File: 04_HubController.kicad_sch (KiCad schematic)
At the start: 79 parts, among them U16 CYUSB3304-68LTXx, Y1 26MHz

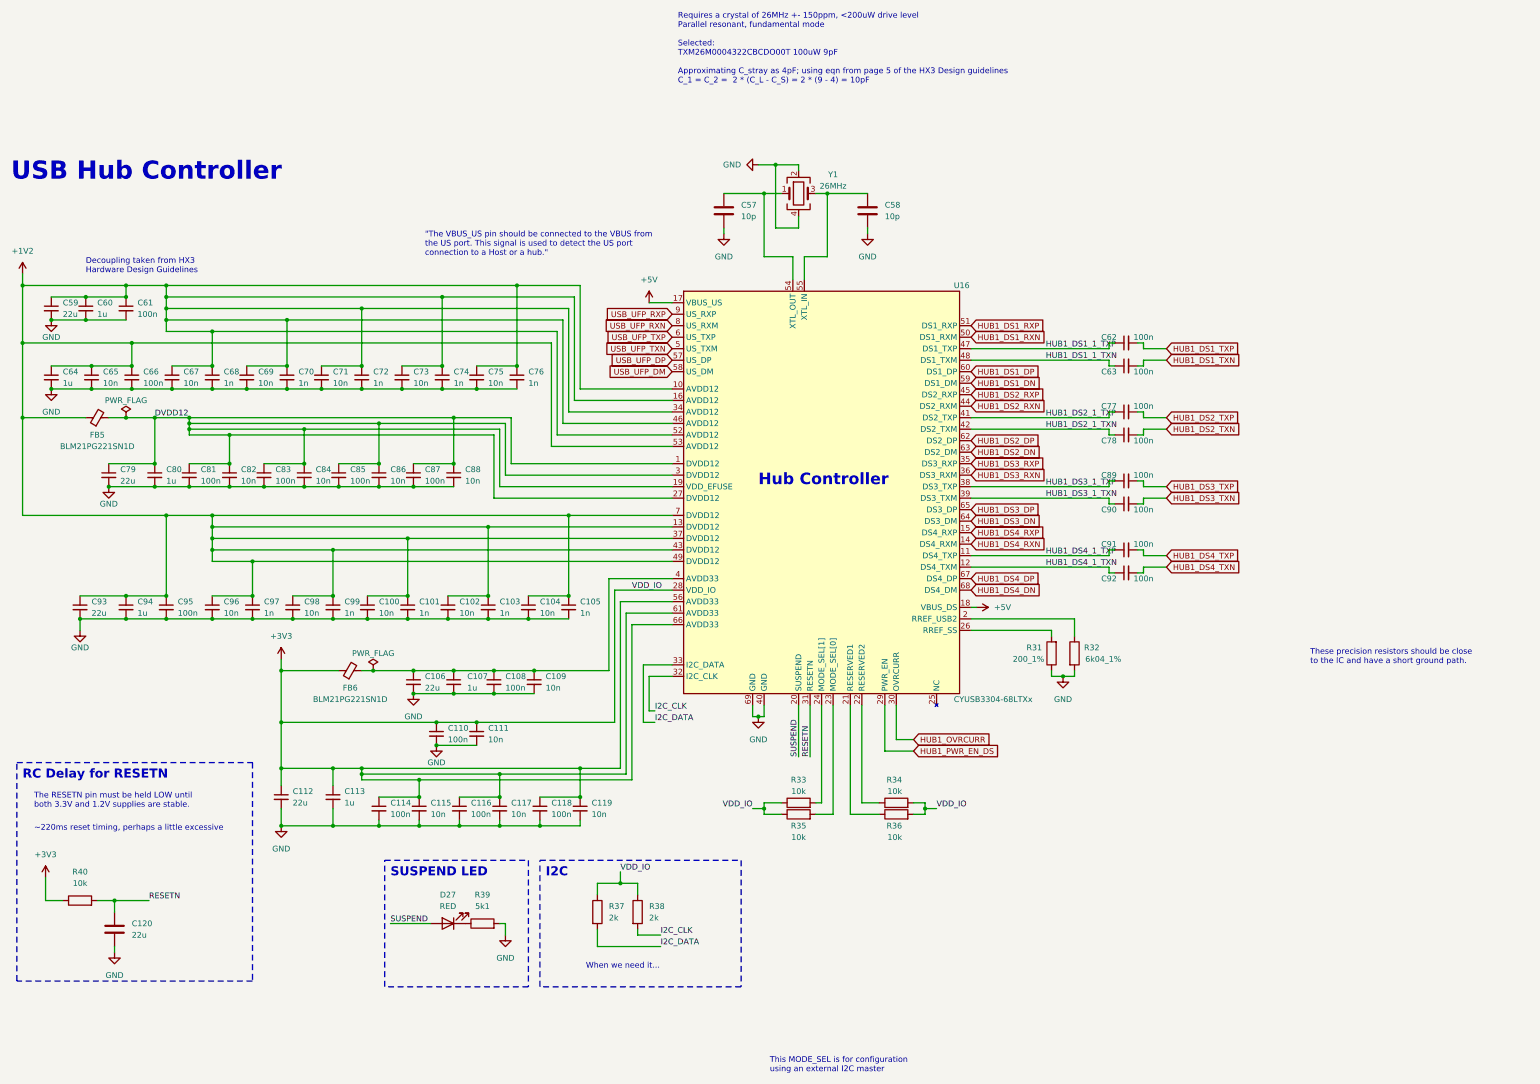
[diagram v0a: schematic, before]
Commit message: route power delivery controller
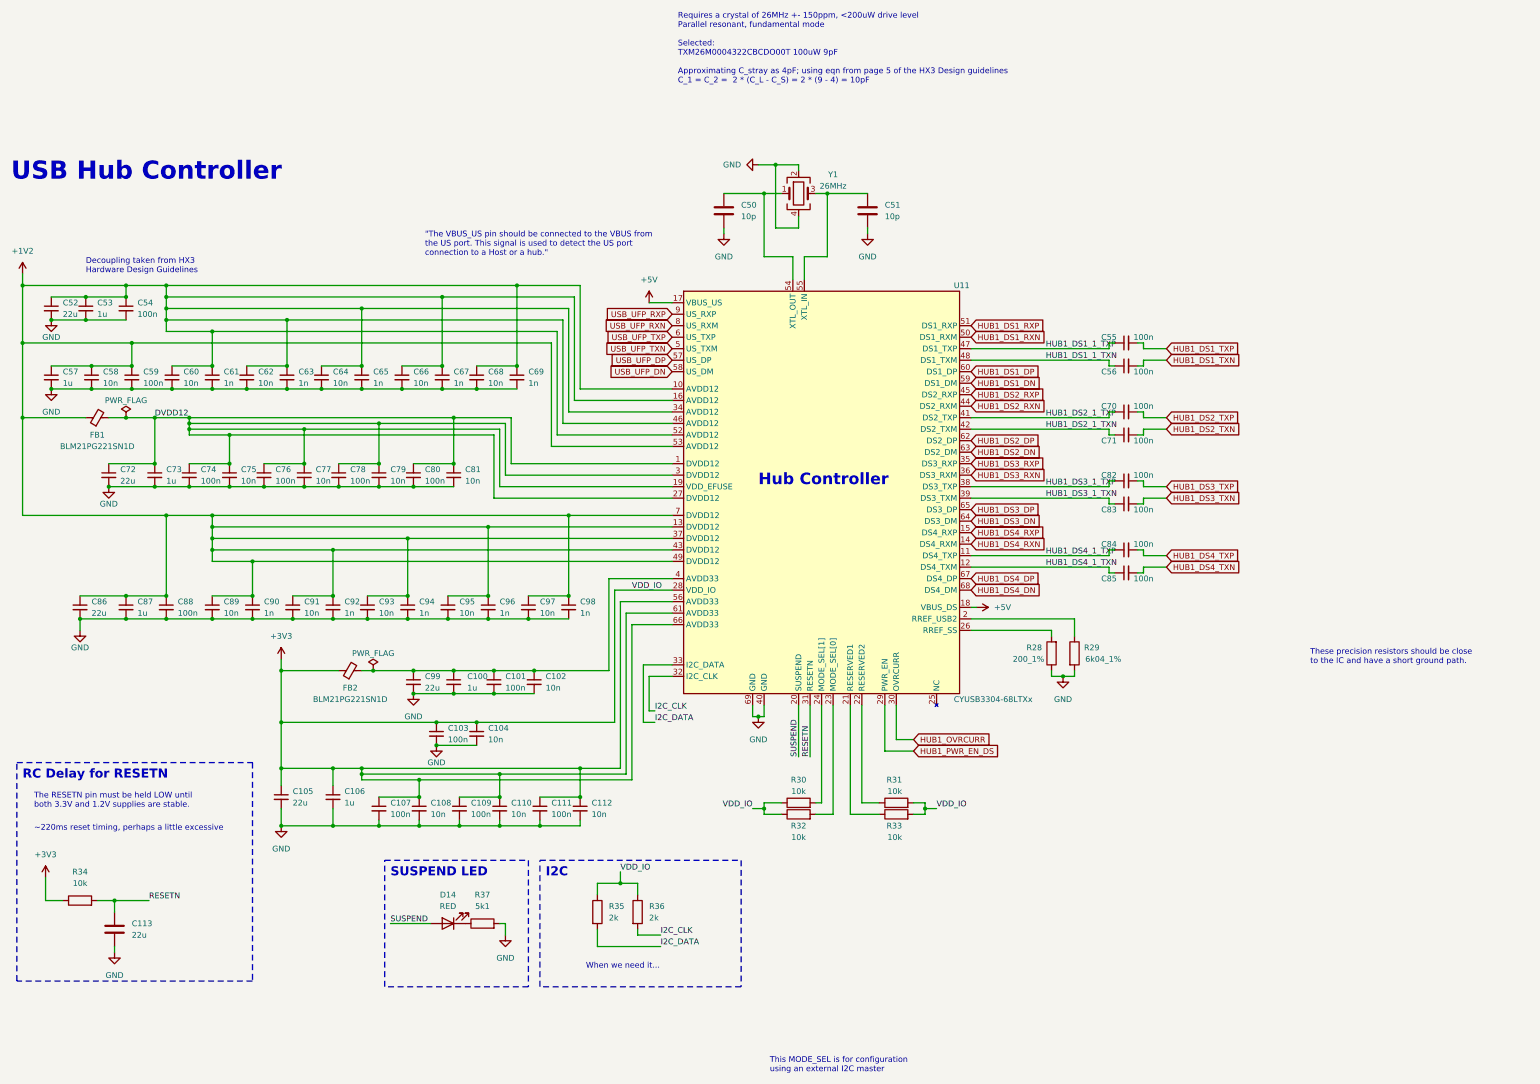
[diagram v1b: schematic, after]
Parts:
- renumbered C107 to C100, C108 to C101, C109 to C102, C110 to C103, C111 to C104, C112 to C105, C113 to C106, C114 to C107, C115 to C108, C116 to C109, C117 to C110, C118 to C111, C119 to C112, C120 to C113, C57 to C50, C58 to C51, C59 to C52, C60 to C53, C61 to C54, C62 to C55, C63 to C56, C64 to C57, C65 to C58, C66 to C59, C67 to C60, C68 to C61, C69 to C62, C70 to C63, C71 to C64, C72 to C65, C73 to C66, C74 to C67, C75 to C68, C76 to C69, C77 to C70, C78 to C71, C79 to C72, C80 to C73, C81 to C74, C82 to C75, C83 to C76, C84 to C77, C85 to C78, C86 to C79, C87 to C80, C88 to C81, C89 to C82, C90 to C83, C91 to C84, C92 to C85, C93 to C86, C94 to C87, C95 to C88, C96 to C89, C97 to C90, C98 to C91, C99 to C92, C100 to C93, C101 to C94, C102 to C95, C103 to C96, C104 to C97, C105 to C98, C106 to C99, D27 to D14, FB5 to FB1, FB6 to FB2, R31 to R28, R32 to R29, R33 to R30, R34 to R31, R35 to R32, R36 to R33, R40 to R34, R37 to R35, R38 to R36, R39 to R37, U16 to U11
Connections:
- net USB_UFP_DM renamed USB_UFP_DN

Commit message: settle on a layout
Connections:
- net HUB1_DS1_RXN: now also U11.51 (DS1_RXP); no longer U11.50 (DS1_RXM)
- net HUB1_DS1_RXP: now also U11.50 (DS1_RXM); no longer U11.51 (DS1_RXP)
- net HUB1_DS2_RXN: now also U11.45 (DS2_RXP); no longer U11.44 (DS2_RXM)
- net HUB1_DS2_RXP: now also U11.44 (DS2_RXM); no longer U11.45 (DS2_RXP)
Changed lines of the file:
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@@
-    )
-  )
-  (global_label "HUB1_DS1_RXN" (shape input) (at 224.79 53.34 0) (fields_autoplaced)
-    (effects (font (size 1.27 1.27)) (justify left))
-    (property "Intersheetrefs" "${INTERSHEET_REFS}" (at 242.3499 53.34 0)
-      (effects (font (size 1.27 1.27)) (justify left) hide)
     )
   )
@@
     )
   )
+  (global_label "HUB1_DS1_RXP" (shape input) (at 224.79 53.34 0) (fields_autoplaced)
+    (effects (font (size 1.27 1.27)) (justify left))
+    (property "Intersheetrefs" "${INTERSHEET_REFS}" (at 242.2894 53.34 0)
+      (effects (font (size 1.27 1.27)) (justify left) hide)
+    )
+  )
   (global_label "HUB1_DS1_DP" (shape input) (at 224.79 60.96 0) (fields_autoplaced)
     (effects (font (size 1.27 1.27)) (justify left))
     (property "Intersheetrefs" "${INTERSHEET_REFS}" (at 241.0799 60.96 0)
-      (effects (font (size 1.27 1.27)) (justify left) hide)
-    )
-  )
-  (global_label "HUB1_DS2_RXN" (shape input) (at 224.79 68.58 0) (fields_autoplaced)
-    (effects (font (size 1.27 1.27)) (justify left))
-    (property "Intersheetrefs" "${INTERSHEET_REFS}" (at 242.3499 68.58 0)
       (effects (font (size 1.27 1.27)) (justify left) hide)
     )
@@
     (property "Intersheetrefs" "${INTERSHEET_REFS}" (at 142.8834 53.34 0)
       (effects (font (size 1.27 1.27)) (justify right) hide)
+    )
+  )
+  (global_label "HUB1_DS1_RXN" (shape input) (at 224.79 50.8 0) (fields_autoplaced)
+    (effects (font (size 1.27 1.27)) (justify left))
+    (property "Intersheetrefs" "${INTERSHEET_REFS}" (at 242.3499 50.8 0)
+      (effects (font (size 1.27 1.27)) (justify left) hide)
+    )
+  )
+  (global_label "HUB1_DS2_RXP" (shape input) (at 224.79 68.58 0) (fields_autoplaced)
+    (effects (font (size 1.27 1.27)) (justify left))
+    (property "Intersheetrefs" "${INTERSHEET_REFS}" (at 242.2894 68.58 0)
+      (effects (font (size 1.27 1.27)) (justify left) hide)
     )
   )
@@
     )
   )
-  (global_label "HUB1_DS1_RXP" (shape input) (at 224.79 50.8 0) (fields_autoplaced)
-    (effects (font (size 1.27 1.27)) (justify left))
-    (property "Intersheetrefs" "${INTERSHEET_REFS}" (at 242.2894 50.8 0)
-      (effects (font (size 1.27 1.27)) (justify left) hide)
-    )
-  )
   (global_label "HUB1_DS2_DP" (shape input) (at 224.79 76.2 0) (fields_autoplaced)
     (effects (font (size 1.27 1.27)) (justify left))
@@
     (effects (font (size 1.27 1.27)) (justify left))
     (property "Intersheetrefs" "${INTERSHEET_REFS}" (at 285.2275 88.9 0)
+      (effects (font (size 1.27 1.27)) (justify left) hide)
+    )
+  )
+  (global_label "HUB1_DS2_RXN" (shape input) (at 224.79 66.04 0) (fields_autoplaced)
+    (effects (font (size 1.27 1.27)) (justify left))
+    (property "Intersheetrefs" "${INTERSHEET_REFS}" (at 242.3499 66.04 0)
       (effects (font (size 1.27 1.27)) (justify left) hide)
     )
@@
       (effects (font (size 1.27 1.27)) (justify left) hide)
     )
-  )
-  (global_label "HUB1_DS2_RXP" (shape input) (at 224.79 66.04 0) (fields_autoplaced)
-    (effects (font (size 1.27 1.27)) (justify left))
-    (property "Intersheetrefs" "${INTERSHEET_REFS}" (at 242.2894 66.04 0)
-      (effects (font (size 1.27 1.27)) (justify left) hide)
-    )

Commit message: finish layout draft
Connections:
- net HUB1_DS4_RXN: now also U11.15 (DS4_RXP); no longer U11.14 (DS4_RXM)
- net HUB1_DS4_RXP: now also U11.14 (DS4_RXM); no longer U11.15 (DS4_RXP)
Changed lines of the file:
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@@
-    )
-  )
-  (global_label "HUB1_DS4_RXN" (shape input) (at 224.79 99.06 0) (fields_autoplaced)
-    (effects (font (size 1.27 1.27)) (justify left))
-    (property "Intersheetrefs" "${INTERSHEET_REFS}" (at 242.3499 99.06 0)
-      (effects (font (size 1.27 1.27)) (justify left) hide)
     )
   )
@@
     )
   )
+  (global_label "HUB1_DS4_RXN" (shape input) (at 224.79 96.52 0) (fields_autoplaced)
+    (effects (font (size 1.27 1.27)) (justify left))
+    (property "Intersheetrefs" "${INTERSHEET_REFS}" (at 242.3499 96.52 0)
+      (effects (font (size 1.27 1.27)) (justify left) hide)
+    )
+  )
   (global_label "HUB1_DS4_DN" (shape input) (at 224.79 109.22 0) (fields_autoplaced)
     (effects (font (size 1.27 1.27)) (justify left))
@@
     )
   )
+  (global_label "HUB1_DS4_RXP" (shape input) (at 224.79 99.06 0) (fields_autoplaced)
+    (effects (font (size 1.27 1.27)) (justify left))
+    (property "Intersheetrefs" "${INTERSHEET_REFS}" (at 242.2894 99.06 0)
+      (effects (font (size 1.27 1.27)) (justify left) hide)
+    )
+  )
   (global_label "HUB1_DS3_RXN" (shape input) (at 224.79 83.82 0) (fields_autoplaced)
     (effects (font (size 1.27 1.27)) (justify left))
     (property "Intersheetrefs" "${INTERSHEET_REFS}" (at 242.3499 83.82 0)
-      (effects (font (size 1.27 1.27)) (justify left) hide)
-    )
-  )
-  (global_label "HUB1_DS4_RXP" (shape input) (at 224.79 96.52 0) (fields_autoplaced)
-    (effects (font (size 1.27 1.27)) (justify left))
-    (property "Intersheetrefs" "${INTERSHEET_REFS}" (at 242.2894 96.52 0)
       (effects (font (size 1.27 1.27)) (justify left) hide)
     )
@@
   )
   (symbol (lib_id "Device:C_Small") (at 100.33 113.03 0) (unit 1)
-    (in_bom yes) (on_board yes) (dnp no) (fields_autoplaced)
+    (in_bom yes) (on_board yes) (dnp no)
     (property "Reference" "C94" (at 102.87 111.7663 0)
-      (effects (font (size 1.27 1.27)) (justify left))
+      (effects (font (size 1.27 1.27)) (justify right))
     )
     (property "Value" "1n" (at 102.87 114.3063 0)

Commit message: fixing drcs
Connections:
- net HUB1_OVRCURR is gone; now on net +3V3: U11.30 (OVRCURR)
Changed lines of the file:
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@@
+    (effects (font (size 1.27 1.27)) (justify left bottom))
+  )
+  (label "VDD_IO" (at 212.09 142.24 0) (fields_autoplaced)
     (effects (font (size 1.27 1.27)) (justify left bottom))
   )
@@
       (effects (font (size 1.27 1.27)) (justify left) hide)
     )
-  )
-  (global_label "HUB1_OVRCURR" (shape input) (at 212.09 142.24 0) (fields_autoplaced)
-    (effects (font (size 1.27 1.27)) (justify left))
-    (property "Intersheetrefs" "${INTERSHEET_REFS}" (at 230.0129 142.24 0)
-      (effects (font (size 1.27 1.27)) (justify left) hide)
-    )

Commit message: finish bom list
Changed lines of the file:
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@@
     (stroke (width 0) (type default))
   )
+  (wire (pts (xy 154.94 45.72) (xy 154.94 44.45))
+    (stroke (width 0) (type default))
+  )
   (wire (pts (xy 138.43 41.91) (xy 124.46 41.91))
     (stroke (width 0) (type default))
@@
     (stroke (width 0) (type default))
   )
-  (wire (pts (xy 153.67 45.72) (xy 158.75 45.72))
-    (stroke (width 0) (type default))
-  )
   (wire (pts (xy 138.43 160.02) (xy 138.43 161.29))
     (stroke (width 0) (type default))
@@
     (stroke (width 0) (type default))
   )
+  (wire (pts (xy 154.94 45.72) (xy 158.75 45.72))
+    (stroke (width 0) (type default))
+  )
   (wire (pts (xy 135.89 92.71) (xy 158.75 92.71))
     (stroke (width 0) (type default))
@@
   )
   (text "\"The VBUS_US pin should be connected to the VBUS from\nthe US port. This signal is used to detect the US port\nconnection to a Host or a hub.\""
-    (at 104.14 35.56 0)
+    (at 101.6 26.67 0)
     (effects (font (size 1.27 1.27)) (justify left bottom))
   )
@@
     )
   )
-  (symbol (lib_id "power:+5V") (at 153.67 45.72 0) (unit 1)
+  (symbol (lib_id "power:+5V") (at 154.94 44.45 0) (unit 1)
     (in_bom yes) (on_board yes) (dnp no) (fields_autoplaced)
-    (property "Reference" "#PWR060" (at 153.67 49.53 0)
+    (property "Reference" "#PWR060" (at 154.94 48.26 0)
       (effects (font (size 1.27 1.27)) hide)
     )
-    (property "Value" "+5V" (at 153.67 40.64 0)
+    (property "Value" "+5V" (at 154.94 39.37 0)
       (effects (font (size 1.27 1.27)))
     )
-    (property "Footprint" "" (at 153.67 45.72 0)
+    (property "Footprint" "" (at 154.94 44.45 0)
       (effects (font (size 1.27 1.27)) hide)
     )
-    (property "Datasheet" "" (at 153.67 45.72 0)
+    (property "Datasheet" "" (at 154.94 44.45 0)
       (effects (font (size 1.27 1.27)) hide)
     )
@@
     )
   )
-  (symbol (lib_id "power:GND") (at 27.94 118.11 0) (unit 1)
+  (symbol (lib_id "power:GND") (at 27.94 118.11 0) (mirror y) (unit 1)
     (in_bom yes) (on_board yes) (dnp no)
     (property "Reference" "#PWR065" (at 27.94 124.46 0)

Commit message: fix bom
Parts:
- added R50, R51: 10k, Resistor_SMD:R_0402_1005Metric, symbol Device:R_Small
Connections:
- net +5V: now also R50.1; no longer U11.17 (VBUS_US)
- net GND: now also R51.2
- new net: R50.2, R51.1, U11.17 (VBUS_US)
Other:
- note added: ""The VBUS_US pin should be connected to the VBUS from the US port. This signal is used to detect the US port connection to a Host or a hub." "It is recommended to connect a pair of resistors to the VBUS_US pin to discharge VBUS faster in case of a disconnection event" HX3 Hardware Design Guidelines page 8."
- note removed: ""The VBUS_US pin should be connected to the VBUS from the US port. This signal is used to detect the US port connection to a Host or a hub.""
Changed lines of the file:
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@@
   (junction (at 77.47 81.28) (diameter 0) (color 0 0 0 0)
   )
+  (junction (at 142.24 34.29) (diameter 0) (color 0 0 0 0)
+  )
   (junction (at 101.6 86.36) (diameter 0) (color 0 0 0 0)
   )
@@
     (stroke (width 0) (type default))
   )
-  (wire (pts (xy 154.94 45.72) (xy 154.94 44.45))
+  (wire (pts (xy 154.94 34.29) (xy 154.94 45.72))
     (stroke (width 0) (type default))
   )
@@
     (stroke (width 0) (type default))
   )
+  (wire (pts (xy 154.94 34.29) (xy 142.24 34.29))
+    (stroke (width 0) (type default))
+  )
   (wire (pts (xy 24.13 177.8) (xy 20.32 177.8))
     (stroke (width 0) (type default))
@@
     (effects (font (size 1.27 1.27)) (justify left bottom))
   )
-  (text "\"The VBUS_US pin should be connected to the VBUS from\nthe US port. This signal is used to detect the US port\nconnection to a Host or a hub.\""
-    (at 101.6 26.67 0)
+  (text "\"The VBUS_US pin should be connected to the VBUS from\nthe US port. This signal is used to detect the US port\nconnection to a Host or a hub.\"\n\n\"It is recommended to connect a pair of resistors \nto the VBUS_US pin to discharge VBUS faster in case \nof a disconnection event\" HX3 Hardware Design Guidelines page 8."
+    (at 68.58 35.56 0)
     (effects (font (size 1.27 1.27)) (justify left bottom))
   )
@@
     )
   )
+  (symbol (lib_id "power:GND") (at 142.24 39.37 0) (unit 1)
+    (in_bom yes) (on_board yes) (dnp no) (fields_autoplaced)
+    (property "Reference" "#PWR060" (at 142.24 45.72 0)
+      (effects (font (size 1.27 1.27)) hide)
+    )
+    (property "Value" "GND" (at 142.24 44.45 0)
+      (effects (font (size 1.27 1.27)))
+    )
+    (property "Footprint" "" (at 142.24 39.37 0)
+      (effects (font (size 1.27 1.27)) hide)
+    )
+    (property "Datasheet" "" (at 142.24 39.37 0)
+      (effects (font (size 1.27 1.27)) hide)
+    )
+    (pin "1")
+    (instances
+      (project "USBHUB"
+        (path "/d5edc647-9ac3-4ac1-ab8a-57c77be3f4d3/ab1e5fbe-3be5-47b1-a048-7835d2aad0d1"
+          (reference "#PWR060") (unit 1)
+        )
+      )
+    )
+  )
   (symbol (lib_id "power:PWR_FLAG") (at 38.1 71.12 0) (unit 1)
     (in_bom yes) (on_board yes) (dnp no)
@@
     )
   )
+  (symbol (lib_id "Device:R_Small") (at 142.24 31.75 0) (unit 1)
+    (in_bom yes) (on_board yes) (dnp no) (fields_autoplaced)
+    (property "Reference" "R50" (at 144.78 30.48 0)
+      (effects (font (size 1.27 1.27)) (justify left))
+    )
+    (property "Value" "10k" (at 144.78 33.02 0)
+      (effects (font (size 1.27 1.27)) (justify left))
+    )
+    (property "Footprint" "Resistor_SMD:R_0402_1005Metric" (at 142.24 31.75 0)
+      (effects (font (size 1.27 1.27)) hide)
+    )
+    (property "Datasheet" "~" (at 142.24 31.75 0)
+      (effects (font (size 1.27 1.27)) hide)
+    )
+    (pin "2")
+    (pin "1")
+    (instances
+      (project "USBHUB"
+        (path "/d5edc647-9ac3-4ac1-ab8a-57c77be3f4d3/ab1e5fbe-3be5-47b1-a048-7835d2aad0d1"
+          (reference "R50") (unit 1)
+        )
+      )
+    )
+  )
+  (symbol (lib_id "Device:R_Small") (at 142.24 36.83 0) (unit 1)
+    (in_bom yes) (on_board yes) (dnp no) (fields_autoplaced)
+    (property "Reference" "R51" (at 144.78 35.56 0)
+      (effects (font (size 1.27 1.27)) (justify left))
+    )
+    (property "Value" "10k" (at 144.78 38.1 0)
+      (effects (font (size 1.27 1.27)) (justify left))
+    )
+    (property "Footprint" "Resistor_SMD:R_0402_1005Metric" (at 142.24 36.83 0)
+      (effects (font (size 1.27 1.27)) hide)
+    )
+    (property "Datasheet" "~" (at 142.24 36.83 0)
+      (effects (font (size 1.27 1.27)) hide)
+    )
+    (pin "2")
+    (pin "1")
+    (instances
+      (project "USBHUB"
+        (path "/d5edc647-9ac3-4ac1-ab8a-57c77be3f4d3/ab1e5fbe-3be5-47b1-a048-7835d2aad0d1"
+          (reference "R51") (unit 1)
+        )
+      )
+    )
+  )
   (symbol (lib_id "Device:C_Small") (at 115.57 62.23 0) (unit 1)
     (in_bom yes) (on_board yes) (dnp no) (fields_autoplaced)
@@
     )
   )
-  (symbol (lib_id "power:+5V") (at 154.94 44.45 0) (unit 1)
-    (in_bom yes) (on_board yes) (dnp no) (fields_autoplaced)
-    (property "Reference" "#PWR060" (at 154.94 48.26 0)
-      (effects (font (size 1.27 1.27)) hide)
-    )
-    (property "Value" "+5V" (at 154.94 39.37 0)
-      (effects (font (size 1.27 1.27)))
-    )
-    (property "Footprint" "" (at 154.94 44.45 0)
-      (effects (font (size 1.27 1.27)) hide)
-    )
-    (property "Datasheet" "" (at 154.94 44.45 0)
-      (effects (font (size 1.27 1.27)) hide)
-    )
-    (pin "1")
-    (instances
-      (project "USBHUB"
-        (path "/d5edc647-9ac3-4ac1-ab8a-57c77be3f4d3/ab1e5fbe-3be5-47b1-a048-7835d2aad0d1"
-          (reference "#PWR060") (unit 1)
-        )
-      )
-    )
-  )
   (symbol (lib_id "Device:C_Small") (at 66.04 113.03 0) (unit 1)
     (in_bom yes) (on_board yes) (dnp no) (fields_autoplaced)
@@
         )
       )
+    )
+  )
+  (symbol (lib_id "power:+5V") (at 142.24 29.21 0) (mirror y) (unit 1)
+    (in_bom yes) (on_board yes) (dnp no)
+    (property "Reference" "#PWR07" (at 142.24 33.02 0)
+      (effects (font (size 1.27 1.27)) hide)
+    )
+    (property "Value" "+5V" (at 142.24 24.13 0)
+      (effects (font (size 1.27 1.27)))
+    )
+    (property "Footprint" "" (at 142.24 29.21 0)
+      (effects (font (size 1.27 1.27)) hide)
+    )
+    (property "Datasheet" "" (at 142.24 29.21 0)
+      (effects (font (size 1.27 1.27)) hide)
+    )
+    (pin "1")
+    (instances
+      (project "USBHUB"
+        (path "/d5edc647-9ac3-4ac1-ab8a-57c77be3f4d3/ab1e5fbe-3be5-47b1-a048-7835d2aad0d1"
+          (reference "#PWR07") (unit 1)
+        )
+      )
